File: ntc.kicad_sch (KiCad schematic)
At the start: 4 parts, among them J10 Conn_01x02_Pin, J11 Conn_01x02_Pin, J12 Conn_01x02_Pin, J13 Conn_01x02_Pin

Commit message: Doing placement
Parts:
- J10, J11, J12, J13: footprint Connector_JST:JST_PH_S2B-PH-SM4-TB_1x02-1MP_P2.00mm_Horizontal -> Connector_JST:JST_GH_SM02B-GHS-TB_1x02-1MP_P1.25mm_Horizontal

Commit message: Pushing
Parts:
- removed J13: Conn_01x02_Pin, Connector_JST:JST_GH_SM02B-GHS-TB_1x02-1MP_P1.25mm_Horizontal, symbol Connector:Conn_01x02_Pin

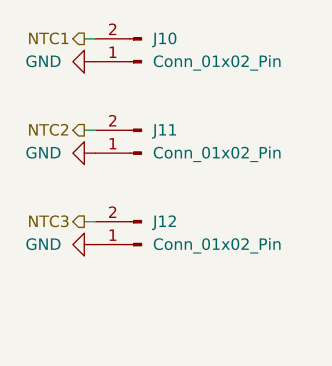
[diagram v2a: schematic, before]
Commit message: Adding in signals and cleaning up schematic
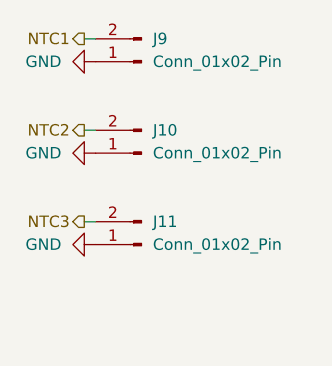
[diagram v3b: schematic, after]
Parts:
- renumbered J11 to J10, J12 to J11, J10 to J9
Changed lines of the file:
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@@
 		(dnp no)
 		(fields_autoplaced yes)
-		(property "Reference" "J11"
+		(property "Reference" "J10"
 			(at 148.59 91.4399 0)
 			(effects
@@
 			(project "BMS"
 				(path "/124184ba-5d68-4d9f-8da6-acc6720ab30b/93f9b420-7cce-46a9-9201-666f07a18f85/b732a1a5-50cf-4d70-be91-0bf27828f771"
-					(reference "J11")
+					(reference "J10")
 					(unit 1)
 				)
@@
 		(dnp no)
 		(fields_autoplaced yes)
-		(property "Reference" "J10"
+		(property "Reference" "J9"
 			(at 148.59 81.2799 0)
 			(effects
@@
 			(project "BMS"
 				(path "/124184ba-5d68-4d9f-8da6-acc6720ab30b/93f9b420-7cce-46a9-9201-666f07a18f85/b732a1a5-50cf-4d70-be91-0bf27828f771"
-					(reference "J10")
+					(reference "J9")
 					(unit 1)
 				)
@@
 		(dnp no)
 		(fields_autoplaced yes)
-		(property "Reference" "J12"
+		(property "Reference" "J11"
 			(at 148.59 101.5999 0)
 			(effects
@@
 			(project "BMS"
 				(path "/124184ba-5d68-4d9f-8da6-acc6720ab30b/93f9b420-7cce-46a9-9201-666f07a18f85/b732a1a5-50cf-4d70-be91-0bf27828f771"
-					(reference "J12")
+					(reference "J11")
 					(unit 1)
 				)
@@
 		(dnp no)
 		(fields_autoplaced yes)
-		(property "Reference" "#PWR071"
+		(property "Reference" "#PWR091"
 			(at 135.89 93.98 0)
 			(effects
@@
 			(project "BMS"
 				(path "/124184ba-5d68-4d9f-8da6-acc6720ab30b/93f9b420-7cce-46a9-9201-666f07a18f85/b732a1a5-50cf-4d70-be91-0bf27828f771"
-					(reference "#PWR071")
+					(reference "#PWR091")
 					(unit 1)
 				)
@@
 		(dnp no)
 		(fields_autoplaced yes)
-		(property "Reference" "#PWR072"
+		(property "Reference" "#PWR092"
 			(at 135.89 104.14 0)
 			(effects
@@
 			(project "BMS"
 				(path "/124184ba-5d68-4d9f-8da6-acc6720ab30b/93f9b420-7cce-46a9-9201-666f07a18f85/b732a1a5-50cf-4d70-be91-0bf27828f771"
-					(reference "#PWR072")
+					(reference "#PWR092")
 					(unit 1)
 				)
@@
 		(dnp no)
 		(fields_autoplaced yes)
-		(property "Reference" "#PWR070"
+		(property "Reference" "#PWR090"
 			(at 135.89 83.82 0)
 			(effects
@@
 			(project ""
 				(path "/124184ba-5d68-4d9f-8da6-acc6720ab30b/93f9b420-7cce-46a9-9201-666f07a18f85/b732a1a5-50cf-4d70-be91-0bf27828f771"
-					(reference "#PWR070")
+					(reference "#PWR090")
 					(unit 1)
 				)

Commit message: prepaing for production
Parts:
- J10, J11, J9: Mfr (none) -> JST; Mfr P/N (none) -> SM02B-GHS-TB(LF)(SN); Supplier_2 (none) -> JLCPCB; Supplier_2 P/N (none) -> C189893
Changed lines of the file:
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@@
 			)
 		)
-		(property "Mfr" ""
-			(at 147.32 93.98 0)
-			(effects
-				(font
-					(size 1.27 1.27)
-				)
-				(hide yes)
-			)
-		)
-		(property "Mfr P/N" ""
+		(property "Mfr" "JST"
+			(at 147.32 93.98 0)
+			(effects
+				(font
+					(size 1.27 1.27)
+				)
+				(hide yes)
+			)
+		)
+		(property "Mfr P/N" "SM02B-GHS-TB(LF)(SN)"
 			(at 147.32 93.98 0)
 			(effects
@@
 			)
 		)
-		(property "Supplier_2" ""
-			(at 147.32 93.98 0)
-			(effects
-				(font
-					(size 1.27 1.27)
-				)
-				(hide yes)
-			)
-		)
-		(property "Supplier_2 P/N" ""
+		(property "Supplier_2" "JLCPCB"
+			(at 147.32 93.98 0)
+			(effects
+				(font
+					(size 1.27 1.27)
+				)
+				(hide yes)
+			)
+		)
+		(property "Supplier_2 P/N" "C189893"
 			(at 147.32 93.98 0)
 			(effects
@@
 		)
 		(property "Supplier_2 Price @ Qty" ""
+			(at 147.32 93.98 0)
+			(effects
+				(font
+					(size 1.27 1.27)
+				)
+				(hide yes)
+			)
+		)
+		(property "DigiKey_Part_Number" ""
 			(at 147.32 93.98 0)
 			(effects
@@
 			)
 		)
-		(property "Mfr" ""
-			(at 147.32 83.82 0)
-			(effects
-				(font
-					(size 1.27 1.27)
-				)
-				(hide yes)
-			)
-		)
-		(property "Mfr P/N" ""
+		(property "Mfr" "JST"
+			(at 147.32 83.82 0)
+			(effects
+				(font
+					(size 1.27 1.27)
+				)
+				(hide yes)
+			)
+		)
+		(property "Mfr P/N" "SM02B-GHS-TB(LF)(SN)"
 			(at 147.32 83.82 0)
 			(effects
@@
 			)
 		)
-		(property "Supplier_2" ""
-			(at 147.32 83.82 0)
-			(effects
-				(font
-					(size 1.27 1.27)
-				)
-				(hide yes)
-			)
-		)
-		(property "Supplier_2 P/N" ""
+		(property "Supplier_2" "JLCPCB"
+			(at 147.32 83.82 0)
+			(effects
+				(font
+					(size 1.27 1.27)
+				)
+				(hide yes)
+			)
+		)
+		(property "Supplier_2 P/N" "C189893"
 			(at 147.32 83.82 0)
 			(effects
@@
 		)
 		(property "Supplier_2 Price @ Qty" ""
+			(at 147.32 83.82 0)
+			(effects
+				(font
+					(size 1.27 1.27)
+				)
+				(hide yes)
+			)
+		)
+		(property "DigiKey_Part_Number" ""
 			(at 147.32 83.82 0)
 			(effects
@@
 			)
 		)
-		(property "Mfr" ""
-			(at 147.32 104.14 0)
-			(effects
-				(font
-					(size 1.27 1.27)
-				)
-				(hide yes)
-			)
-		)
-		(property "Mfr P/N" ""
+		(property "Mfr" "JST"
+			(at 147.32 104.14 0)
+			(effects
+				(font
+					(size 1.27 1.27)
+				)
+				(hide yes)
+			)
+		)
+		(property "Mfr P/N" "SM02B-GHS-TB(LF)(SN)"
 			(at 147.32 104.14 0)
 			(effects
@@
 			)
 		)
-		(property "Supplier_2" ""
-			(at 147.32 104.14 0)
-			(effects
-				(font
-					(size 1.27 1.27)
-				)
-				(hide yes)
-			)
-		)
-		(property "Supplier_2 P/N" ""
+		(property "Supplier_2" "JLCPCB"
+			(at 147.32 104.14 0)
+			(effects
+				(font
+					(size 1.27 1.27)
+				)
+				(hide yes)
+			)
+		)
+		(property "Supplier_2 P/N" "C189893"
 			(at 147.32 104.14 0)
 			(effects
@@
 		)
 		(property "Supplier_2 Price @ Qty" ""
+			(at 147.32 104.14 0)
+			(effects
+				(font
+					(size 1.27 1.27)
+				)
+				(hide yes)
+			)
+		)
+		(property "DigiKey_Part_Number" ""
 			(at 147.32 104.14 0)
 			(effects
@@
 		(dnp no)
 		(fields_autoplaced yes)
-		(property "Reference" "#PWR091"
+		(property "Reference" "#PWR093"
 			(at 135.89 93.98 0)
 			(effects
@@
 			(project "BMS"
 				(path "/124184ba-5d68-4d9f-8da6-acc6720ab30b/93f9b420-7cce-46a9-9201-666f07a18f85/b732a1a5-50cf-4d70-be91-0bf27828f771"
-					(reference "#PWR091")
+					(reference "#PWR093")
 					(unit 1)
 				)
@@
 		(dnp no)
 		(fields_autoplaced yes)
-		(property "Reference" "#PWR092"
+		(property "Reference" "#PWR094"
 			(at 135.89 104.14 0)
 			(effects
@@
 			(project "BMS"
 				(path "/124184ba-5d68-4d9f-8da6-acc6720ab30b/93f9b420-7cce-46a9-9201-666f07a18f85/b732a1a5-50cf-4d70-be91-0bf27828f771"
-					(reference "#PWR092")
+					(reference "#PWR094")
 					(unit 1)
 				)
@@
 		(dnp no)
 		(fields_autoplaced yes)
-		(property "Reference" "#PWR090"
+		(property "Reference" "#PWR092"
 			(at 135.89 83.82 0)
 			(effects
@@
 			(project ""
 				(path "/124184ba-5d68-4d9f-8da6-acc6720ab30b/93f9b420-7cce-46a9-9201-666f07a18f85/b732a1a5-50cf-4d70-be91-0bf27828f771"
-					(reference "#PWR090")
+					(reference "#PWR092")
 					(unit 1)
 				)
